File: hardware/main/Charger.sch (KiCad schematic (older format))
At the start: 74 parts, among them K801 DIPxx-1Axx-13x, K802 SANYOU_SRD_Form_C, Q801 BCV27, Q802 Q_NPN_BEC, Q803 BCV27, U801 LM7812

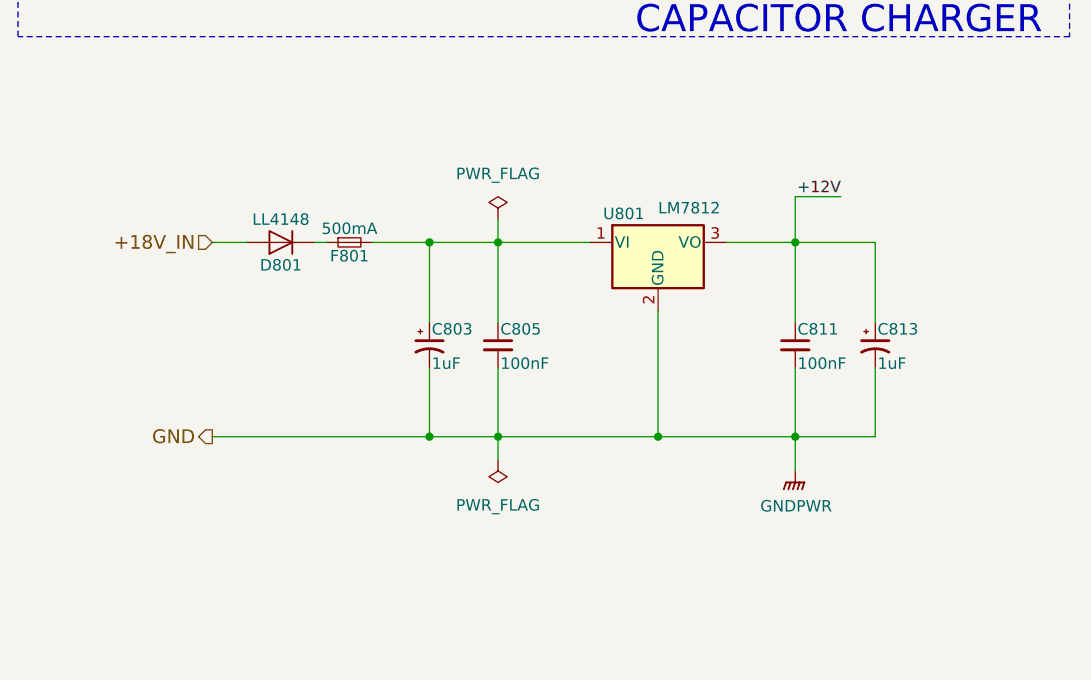
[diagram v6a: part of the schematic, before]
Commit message: Copper bar fixation
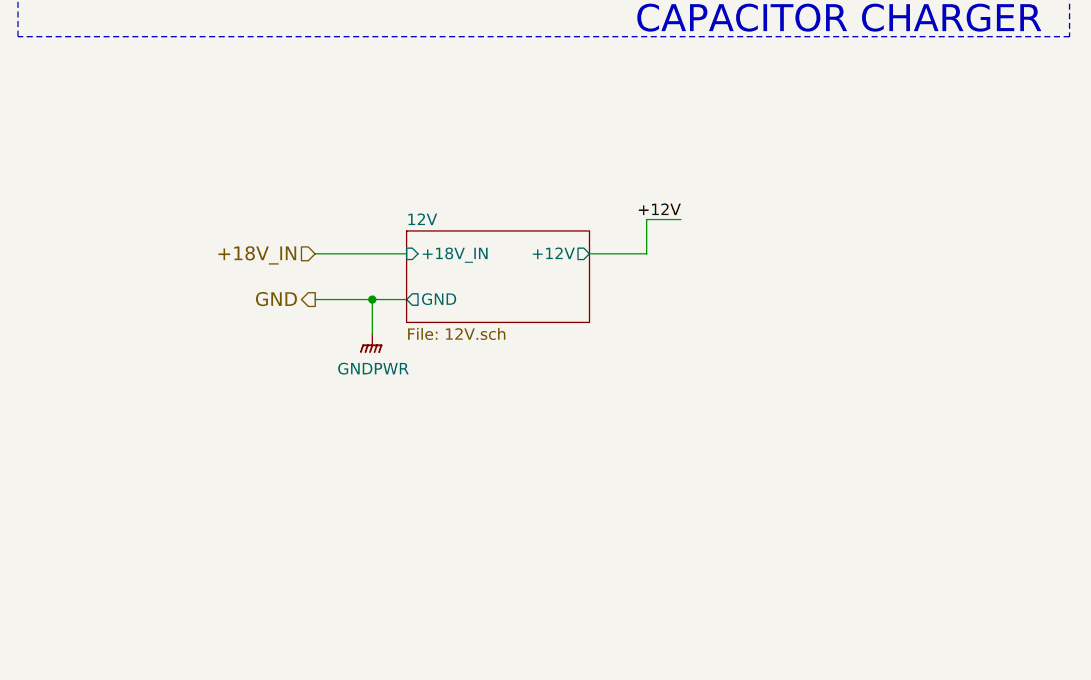
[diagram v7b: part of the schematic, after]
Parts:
- removed C803: 1uF, Capacitor_SMD:C_0805_2012Metric_Pad1.15x1.40mm_HandSolder, symbol Device:CP1_Small
- removed C805, C811: 100nF, Capacitor_SMD:C_0805_2012Metric_Pad1.15x1.40mm_HandSolder, symbol Device:C_Small
- removed C813: 1uF, Capacitor_Tantalum_SMD:CP_EIA-6032-20_AVX-F_Pad2.25x2.35mm_HandSolder, symbol Device:CP1_Small
- removed D801: LL4148, Diode_SMD:D_MiniMELF_Handsoldering, symbol Diode:LL4148
- removed F801: 500mA, Fuse:Fuse_1206_3216Metric_Pad1.42x1.75mm_HandSolder, symbol Device:Fuse_Small
- removed U801: LM7812, Package_SO:SOIC-8_3.9x4.9mm_P1.27mm, symbol Regulator_Linear:LM7805_TO220
- C812: footprint Capacitor_SMD:C_0805_2012Metric_Pad1.15x1.40mm_HandSolder -> Capacitor_THT:CP_Radial_D10.0mm_P5.00mm
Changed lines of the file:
@@
 $Descr A3 16535 11693
 encoding utf-8
-Sheet 2 8
+Sheet 2 9
 Title ""
 Date ""
@@
 F 0 "C812" H 4250 5300 50  0000 L CNN
 F 1 "4700u" H 4250 5250 50  0000 L CNN
-F 2 "Capacitor_SMD:C_0805_2012Metric_Pad1.15x1.40mm_HandSolder" H 4150 5250 50  0001 C CNN
+F 2 "Capacitor_THT:CP_Radial_D10.0mm_P5.00mm" H 4150 5250 50  0001 C CNN
 F 3 "~" H 4150 5250 50  0001 C CNN
 	1    4150 5250
@@
 Wire Wire Line
 	2800 3100 2800 3450
-$Comp
-L Regulator_Linear:LM7805_TO220 U?
-U 1 1 5CB0F970
-P 3450 7600
-AR Path="/5AACFFEF/5CB0F970" Ref="U?"  Part="1"
-AR Path="/5CA4DC1F/5CA5A5C0/5CB0F970" Ref="U?"  Part="1"
-AR Path="/5C9C4D6B/5CB0F970" Ref="U801"  Part="1"
-AR Path="/5CBD2CE3/5CB0F970" Ref="U?"  Part="1"
-F 0 "U801" H 3300 7725 50  0000 C CNN
-F 1 "LM7812" H 3450 7750 50  0000 L CNN
-F 2 "Package_SO:SOIC-8_3.9x4.9mm_P1.27mm" H 3450 7825 50  0001 C CIN
-F 3 "https://www.sparkfun.com/datasheets/Components/LM7805.pdf" H 3450 7550 50  0001 C CNN
-	1    3450 7600
-	1    0    0    -1
-$EndComp
-Text HLabel 1500 8450 0    60   Output ~ 0
+Text HLabel 1950 7850 0    60   Output ~ 0
 GND
-$Comp
-L Device:C_Small C?
-U 1 1 5CB0F97E
-P 2750 8050
-AR Path="/5AACFFEF/5CB0F97E" Ref="C?"  Part="1"
-AR Path="/5CA4DC1F/5CA5A5C0/5CB0F97E" Ref="C?"  Part="1"
-AR Path="/5C9C4D6B/5CB0F97E" Ref="C805"  Part="1"
-AR Path="/5CBD2CE3/5CB0F97E" Ref="C?"  Part="1"
-F 0 "C805" H 2760 8120 50  0000 L CNN
-F 1 "100nF" H 2760 7970 50  0000 L CNN
-F 2 "Capacitor_SMD:C_0805_2012Metric_Pad1.15x1.40mm_HandSolder" H 2750 8050 50  0001 C CNN
-F 3 "" H 2750 8050 50  0001 C CNN
-	1    2750 8050
-	1    0    0    -1
-$EndComp
-$Comp
-L Diode:LL4148 D?
-U 1 1 5CB0F984
-P 1800 7600
-AR Path="/5AACFFEF/5CB0F984" Ref="D?"  Part="1"
-AR Path="/5CA4DC1F/5CA5A5C0/5CB0F984" Ref="D?"  Part="1"
-AR Path="/5C9C4D6B/5CB0F984" Ref="D801"  Part="1"
-AR Path="/5CBD2CE3/5CB0F984" Ref="D?"  Part="1"
-F 0 "D801" H 1800 7700 50  0000 C CNN
-F 1 "LL4148" H 1800 7500 50  0000 C CNN
-F 2 "Diode_SMD:D_MiniMELF_Handsoldering" H 1800 7425 50  0001 C CNN
-F 3 "https://www.vishay.com/docs/85557/ll4148.pdf" H 1800 7600 50  0001 C CNN
-	1    1800 7600
-	-1   0    0    1
-$EndComp
-Text HLabel 1500 7600 0    60   Input ~ 0
+Text HLabel 1950 7650 0    60   Input ~ 0
 +18V_IN
-$Comp
-L Device:C_Small C?
-U 1 1 5CB0F98B
-P 4050 8050
-AR Path="/5AACFFEF/5CB0F98B" Ref="C?"  Part="1"
-AR Path="/5CA4DC1F/5CA5A5C0/5CB0F98B" Ref="C?"  Part="1"
-AR Path="/5C9C4D6B/5CB0F98B" Ref="C811"  Part="1"
-AR Path="/5CBD2CE3/5CB0F98B" Ref="C?"  Part="1"
-F 0 "C811" H 4060 8120 50  0000 L CNN
-F 1 "100nF" H 4060 7970 50  0000 L CNN
-F 2 "Capacitor_SMD:C_0805_2012Metric_Pad1.15x1.40mm_HandSolder" H 4050 8050 50  0001 C CNN
-F 3 "" H 4050 8050 50  0001 C CNN
-	1    4050 8050
-	1    0    0    -1
-$EndComp
-$Comp
-L Device:Fuse_Small F?
-U 1 1 5CB0F997
-P 2100 7600
-AR Path="/5AACFFEF/5CB0F997" Ref="F?"  Part="1"
-AR Path="/5CA4DC1F/5CA5A5C0/5CB0F997" Ref="F?"  Part="1"
-AR Path="/5C9C4D6B/5CB0F997" Ref="F801"  Part="1"
-AR Path="/5CBD2CE3/5CB0F997" Ref="F?"  Part="1"
-F 0 "F801" H 2100 7540 50  0000 C CNN
-F 1 "500mA" H 2100 7660 50  0000 C CNN
-F 2 "Fuse:Fuse_1206_3216Metric_Pad1.42x1.75mm_HandSolder" H 2100 7600 50  0001 C CNN
-F 3 "https://www.mouser.com/datasheet/2/643/0ZCJ_Nov2016-1132002.pdf" H 2100 7600 50  0001 C CNN
-	1    2100 7600
-	1    0    0    -1
-$EndComp
-Wire Wire Line
-	2450 8450 2450 8150
-Connection ~ 2450 7600
-Wire Wire Line
-	2750 8150 2750 8450
-Connection ~ 2450 8450
-Connection ~ 2750 7600
-Wire Wire Line
-	1650 7600 1500 7600
-Connection ~ 2750 8450
-Wire Wire Line
-	3450 8450 3450 7900
-Wire Wire Line
-	4050 8450 4050 8150
-Connection ~ 3450 8450
-Connection ~ 4050 7600
-Wire Wire Line
-	1500 8450 2450 8450
-Wire Wire Line
-	4400 7600 4400 7950
-Wire Wire Line
-	4400 8450 4400 8150
-Connection ~ 4050 8450
-Wire Wire Line
-	2450 7600 2450 7950
-Wire Wire Line
-	2200 7600 2450 7600
-Wire Wire Line
-	2450 7600 2750 7600
-Wire Wire Line
-	2450 8450 2750 8450
-Wire Wire Line
-	2750 7600 2750 7950
-Wire Wire Line
-	2750 7600 3150 7600
-Wire Wire Line
-	2750 8450 2750 8550
-Wire Wire Line
-	2750 8450 3450 8450
-Wire Wire Line
-	3450 8450 4050 8450
-Wire Wire Line
-	4050 7600 4400 7600
-Wire Wire Line
-	4050 7600 4050 7950
-Wire Wire Line
-	4050 8450 4400 8450
-Wire Wire Line
-	1950 7600 2000 7600
-$Comp
-L power:PWR_FLAG #FLG?
-U 1 1 5CB0F9BC
-P 2750 7500
-AR Path="/5AACFFEF/5CB0F9BC" Ref="#FLG?"  Part="1"
-AR Path="/5CA4DC1F/5CA5A5C0/5CB0F9BC" Ref="#FLG?"  Part="1"
-AR Path="/5C9C4D6B/5CB0F9BC" Ref="#FLG0802"  Part="1"
-AR Path="/5CBD2CE3/5CB0F9BC" Ref="#FLG?"  Part="1"
-F 0 "#FLG0802" H 2750 7575 50  0001 C CNN
-F 1 "PWR_FLAG" H 2750 7700 50  0000 C CNN
-F 2 "" H 2750 7500 50  0001 C CNN
-F 3 "~" H 2750 7500 50  0001 C CNN
-	1    2750 7500
-	1    0    0    -1
-$EndComp
-$Comp
-L power:PWR_FLAG #FLG?
-U 1 1 5CB0F9C2
-P 2750 8550
-AR Path="/5AACFFEF/5CB0F9C2" Ref="#FLG?"  Part="1"
-AR Path="/5CA4DC1F/5CA5A5C0/5CB0F9C2" Ref="#FLG?"  Part="1"
-AR Path="/5C9C4D6B/5CB0F9C2" Ref="#FLG0803"  Part="1"
-AR Path="/5CBD2CE3/5CB0F9C2" Ref="#FLG?"  Part="1"
-F 0 "#FLG0803" H 2750 8625 50  0001 C CNN
-F 1 "PWR_FLAG" H 2750 8750 50  0000 C CNN
-F 2 "" H 2750 8550 50  0001 C CNN
-F 3 "~" H 2750 8550 50  0001 C CNN
-	1    2750 8550
-	-1   0    0    1
-$EndComp
-Wire Wire Line
-	2750 7500 2750 7600
-$Comp
-L Device:CP1_Small C?
-U 1 1 5CB0F978
-P 2450 8050
-AR Path="/5AACFFEF/5CB0F978" Ref="C?"  Part="1"
-AR Path="/5CA4DC1F/5CA5A5C0/5CB0F978" Ref="C?"  Part="1"
-AR Path="/5C9C4D6B/5CB0F978" Ref="C803"  Part="1"
-AR Path="/5CBD2CE3/5CB0F978" Ref="C?"  Part="1"
-F 0 "C803" H 2460 8120 50  0000 L CNN
-F 1 "1uF" H 2460 7970 50  0000 L CNN
-F 2 "Capacitor_SMD:C_0805_2012Metric_Pad1.15x1.40mm_HandSolder" H 2450 8050 50  0001 C CNN
-F 3 "" H 2450 8050 50  0001 C CNN
-	1    2450 8050
-	1    0    0    -1
-$EndComp
-$Comp
-L Device:CP1_Small C?
-U 1 1 5CB0F991
-P 4400 8050
-AR Path="/5AACFFEF/5CB0F991" Ref="C?"  Part="1"
-AR Path="/5CA4DC1F/5CA5A5C0/5CB0F991" Ref="C?"  Part="1"
-AR Path="/5C9C4D6B/5CB0F991" Ref="C813"  Part="1"
-AR Path="/5CBD2CE3/5CB0F991" Ref="C?"  Part="1"
-F 0 "C813" H 4410 8120 50  0000 L CNN
-F 1 "1uF" H 4410 7970 50  0000 L CNN
-F 2 "Capacitor_Tantalum_SMD:CP_EIA-6032-20_AVX-F_Pad2.25x2.35mm_HandSolder" H 4400 8050 50  0001 C CNN
-F 3 "" H 4400 8050 50  0001 C CNN
-	1    4400 8050
-	1    0    0    -1
-$EndComp
-Wire Wire Line
-	4250 7400 4050 7400
-Wire Wire Line
-	4050 7400 4050 7600
-Text Label 4250 7400 2    50   ~ 0
-+12V
 Wire Wire Line
 	7700 4900 7700 5250
-$Comp
-L power:GNDPWR #PWR0804
-U 1 1 5CB769FE
-P 4050 8600
-AR Path="/5C9C4D6B/5CB769FE" Ref="#PWR0804"  Part="1"
-AR Path="/5CBD2CE3/5CB769FE" Ref="#PWR?"  Part="1"
-F 0 "#PWR0804" H 4050 8400 50  0001 C CNN
-F 1 "GNDPWR" H 4054 8446 50  0000 C CNN
-F 2 "" H 4050 8550 50  0001 C CNN
-F 3 "" H 4050 8550 50  0001 C CNN
-	1    4050 8600
-	1    0    0    -1
-$EndComp
-Wire Wire Line
-	4050 8600 4050 8450
 $Comp
 L power:PWR_FLAG #FLG0801
@@
 Wire Wire Line
 	1950 2600 2050 2600
-Wire Wire Line
-	3750 7600 4050 7600
 $Comp
 L power:PWR_FLAG #FLG0101
@@
 	1    0    0    -1
 $EndComp
+$Sheet
+S 2350 7550 800  400
+U 5CA70307
+F0 "12V" 50
+F1 "12V.sch" 50
+F2 "+18V_IN" I L 2350 7650 50
+F3 "GND" O L 2350 7850 50
+F4 "+12V" O R 3150 7650 50
+$EndSheet
+Wire Wire Line
+	1950 7850 2200 7850
+$Comp
+L power:GNDPWR #PWR?
+U 1 1 5CA8D58E
+P 2200 8000
+AR Path="/5C9C4D6B/5CA8D58E" Ref="#PWR?"  Part="1"
+AR Path="/5CBD2CE3/5CA8D58E" Ref="#PWR?"  Part="1"
+F 0 "#PWR?" H 2200 7800 50  0001 C CNN
+F 1 "GNDPWR" H 2204 7846 50  0000 C CNN
+F 2 "" H 2200 7950 50  0001 C CNN
+F 3 "" H 2200 7950 50  0001 C CNN
+	1    2200 8000
+	1    0    0    -1
+$EndComp
+Wire Wire Line
+	2200 8000 2200 7850
+Connection ~ 2200 7850
+Wire Wire Line
+	2200 7850 2350 7850
+Wire Wire Line
+	1950 7650 2350 7650
+Wire Wire Line
+	3150 7650 3400 7650
+Wire Wire Line
+	3400 7650 3400 7500
+Wire Wire Line
+	3400 7500 3550 7500
+Text Label 3550 7500 2    50   ~ 0
++12V
 $EndSCHEMATC

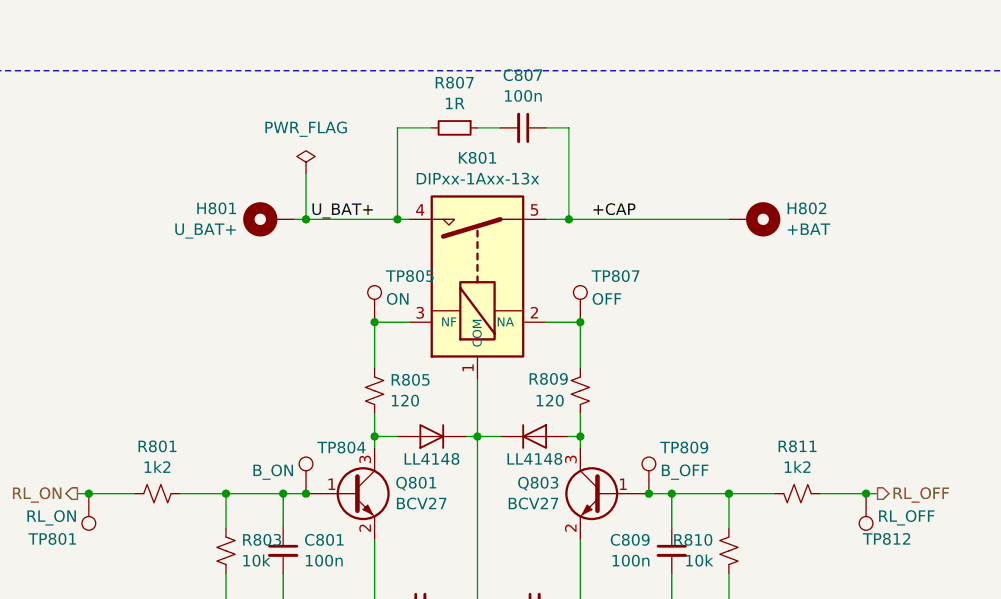
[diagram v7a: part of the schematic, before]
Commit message: Layout and Relay footprint
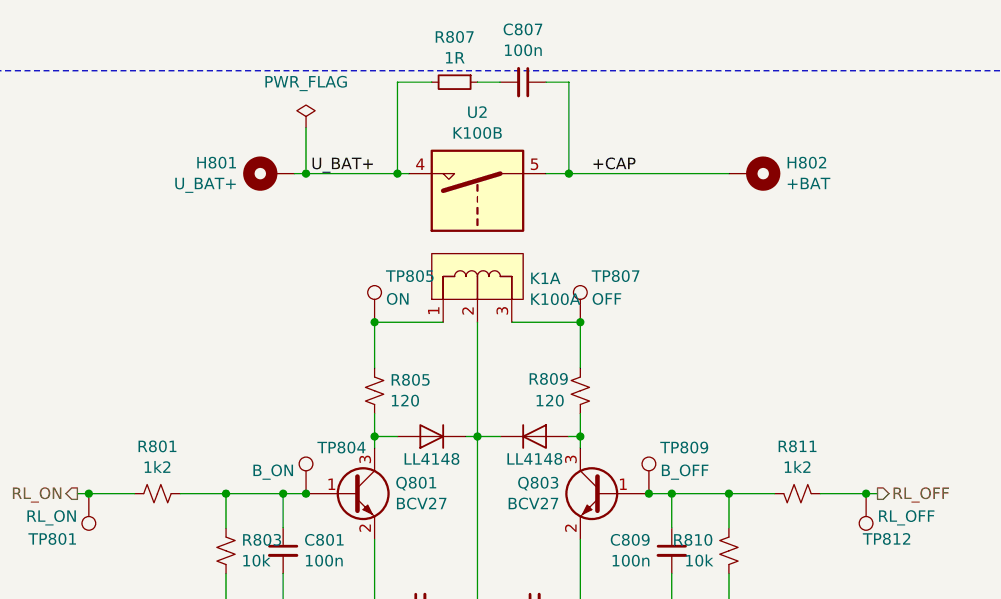
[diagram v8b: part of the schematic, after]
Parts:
- removed K801: DIPxx-1Axx-13x, KicadZeniteSolarLibrary18:Mega_Relay_K100, symbol main-rescue:DIPxx-1Axx-13x-High_current_rele
- added K1: K100A, Connector_PinHeader_2.54mm:PinHeader_1x03_P2.54mm_Vertical_SMD_Pin1Right, symbol K100:K100A
- added U2: K100B, KicadZeniteSolarLibrary18:Mega_Relay_K100_separated, symbol k100A:K100B
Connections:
- net +12V: now also K1.2
- net +CAP: now also U2.5
- net U_BAT+: now also U2.4
- net at R809.1, TP807.1: now also K1.3
- net at R805.1, TP805.1: now also K1.1
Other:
- moved on the sheet: C807, H801, H802, R807
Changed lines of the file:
@@
-$EndComp
-$Comp
-L main-rescue:DIPxx-1Axx-13x-High_current_rele K?
-U 1 1 5C9E2F33
-P 2800 1600
-AR Path="/5C9E2F33" Ref="K?"  Part="1"
-AR Path="/5C9C4D6B/5C9E2F33" Ref="K801"  Part="1"
-AR Path="/5CBD2CE3/5C9E2F33" Ref="K?"  Part="1"
-F 0 "K801" V 3267 1600 50  0000 C CNN
-F 1 "DIPxx-1Axx-13x" V 3176 1600 50  0000 C CNN
-F 2 "KicadZeniteSolarLibrary18:Mega_Relay_K100" H 3150 1550 50  0001 L CNN
-F 3 "https://standexelectronics.com/wp-content/uploads/datasheet_reed_relay_DIP.pdf" H 2800 1600 50  0001 C CNN
-	1    2800 1600
-	0    -1   -1   0
 $EndComp
 $Comp
@@
 	2350 2050 2350 1850
 Wire Wire Line
-	2350 1850 2500 1850
-Wire Wire Line
 	2350 2250 2350 2350
 $Comp
@@
 	3250 2050 3250 1850
 Wire Wire Line
-	3250 1850 3100 1850
-Wire Wire Line
 	3250 2250 3250 2350
 $Comp
@@
 Wire Wire Line
 	3650 3150 3650 3100
-Text Label 2350 1400 2    50   ~ 0
+Text Label 2350 1200 2    50   ~ 0
 U_BAT+
 $Comp
 L Mechanical:MountingHole_Pad H802
 U 1 1 5C9E3AC0
-P 4000 1400
+P 4000 1200
 AR Path="/5C9C4D6B/5C9E3AC0" Ref="H802"  Part="1"
 AR Path="/5CBD2CE3/5C9E3AC0" Ref="H?"  Part="1"
-F 0 "H802" V 3954 1550 50  0000 L CNN
-F 1 "+BAT" V 4045 1550 50  0000 L CNN
-F 2 "MountingHole:MountingHole_3.2mm_M3_DIN965_Pad" H 4000 1400 50  0001 C CNN
-F 3 "~" H 4000 1400 50  0001 C CNN
-	1    4000 1400
+F 0 "H802" V 3954 1350 50  0000 L CNN
+F 1 "+BAT" V 4045 1350 50  0000 L CNN
+F 2 "MountingHole:MountingHole_3.2mm_M3_DIN965_Pad" H 4000 1200 50  0001 C CNN
+F 3 "~" H 4000 1200 50  0001 C CNN
+	1    4000 1200
 	0    1    1    0
 $EndComp
@@
 L Mechanical:MountingHole_Pad H801
 U 1 1 5CA4A13E
-P 1900 1400
+P 1900 1200
 AR Path="/5C9C4D6B/5CA4A13E" Ref="H801"  Part="1"
 AR Path="/5CBD2CE3/5CA4A13E" Ref="H?"  Part="1"
-F 0 "H801" V 1854 1550 50  0000 L CNN
-F 1 "U_BAT+" V 1945 1550 50  0000 L CNN
-F 2 "MountingHole:MountingHole_3.2mm_M3_DIN965_Pad" H 1900 1400 50  0001 C CNN
-F 3 "~" H 1900 1400 50  0001 C CNN
-	1    1900 1400
+F 0 "H801" V 1854 1350 50  0000 L CNN
+F 1 "U_BAT+" V 1945 1350 50  0000 L CNN
+F 2 "MountingHole:MountingHole_3.2mm_M3_DIN965_Pad" H 1900 1200 50  0001 C CNN
+F 3 "~" H 1900 1200 50  0001 C CNN
+	1    1900 1200
 	0    -1   1    0
 $EndComp
@@
 $EndComp
 Wire Wire Line
-	2000 1400 2050 1400
+	2000 1200 2050 1200
 $Comp
 L power:GNDPWR #PWR0810
@@
 Wire Wire Line
 	4150 5450 4150 5500
-Wire Wire Line
-	2800 2100 2800 2350
 Text Label 3000 3450 2    50   ~ 0
 +12V
@@
 L power:PWR_FLAG #FLG0801
 U 1 1 5CB83AF7
-P 2050 1200
+P 2050 1000
 AR Path="/5C9C4D6B/5CB83AF7" Ref="#FLG0801"  Part="1"
 AR Path="/5CBD2CE3/5CB83AF7" Ref="#FLG?"  Part="1"
-F 0 "#FLG0801" H 2050 1275 50  0001 C CNN
-F 1 "PWR_FLAG" H 2050 1400 50  0000 C CNN
-F 2 "" H 2050 1200 50  0001 C CNN
-F 3 "~" H 2050 1200 50  0001 C CNN
-	1    2050 1200
-	1    0    0    -1
-$EndComp
-Wire Wire Line
-	2050 1200 2050 1400
-Connection ~ 2050 1400
-Wire Wire Line
-	2050 1400 2450 1400
+F 0 "#FLG0801" H 2050 1075 50  0001 C CNN
+F 1 "PWR_FLAG" H 2050 1200 50  0000 C CNN
+F 2 "" H 2050 1000 50  0001 C CNN
+F 3 "~" H 2050 1000 50  0001 C CNN
+	1    2050 1000
+	1    0    0    -1
+$EndComp
+Wire Wire Line
+	2050 1000 2050 1200
+Connection ~ 2050 1200
+Wire Wire Line
+	2050 1200 2450 1200
 $Comp
 L power:PWR_FLAG #FLG0804
@@
 L Device:R_Small R807
 U 1 1 5CA4B635
-P 2700 1000
-F 0 "R807" V 2504 1000 50  0000 C CNN
-F 1 "1R" V 2595 1000 50  0000 C CNN
-F 2 "Resistor_SMD:R_0805_2012Metric_Pad1.15x1.40mm_HandSolder" H 2700 1000 50  0001 C CNN
-F 3 "~" H 2700 1000 50  0001 C CNN
-	1    2700 1000
+P 2700 800
+F 0 "R807" V 2504 800 50  0000 C CNN
+F 1 "1R" V 2595 800 50  0000 C CNN
+F 2 "Resistor_SMD:R_0805_2012Metric_Pad1.15x1.40mm_HandSolder" H 2700 800 50  0001 C CNN
+F 3 "~" H 2700 800 50  0001 C CNN
+	1    2700 800
 	0    1    1    0
 $EndComp
@@
 L Device:C_Small C807
 U 1 1 5CA4B63B
-P 3000 1000
-F 0 "C807" V 2771 1000 50  0000 C CNN
-F 1 "100n" V 2862 1000 50  0000 C CNN
-F 2 "Capacitor_SMD:C_0805_2012Metric_Pad1.15x1.40mm_HandSolder" H 3000 1000 50  0001 C CNN
-F 3 "~" H 3000 1000 50  0001 C CNN
-	1    3000 1000
+P 3000 800
+F 0 "C807" V 2771 800 50  0000 C CNN
+F 1 "100n" V 2862 800 50  0000 C CNN
+F 2 "Capacitor_SMD:C_0805_2012Metric_Pad1.15x1.40mm_HandSolder" H 3000 800 50  0001 C CNN
+F 3 "~" H 3000 800 50  0001 C CNN
+	1    3000 800
 	0    1    1    0
 $EndComp
 Wire Wire Line
-	2800 1000 2900 1000
-Wire Wire Line
-	2450 1000 2450 1400
-Wire Wire Line
-	2450 1000 2600 1000
-Connection ~ 2450 1400
-Wire Wire Line
-	2450 1400 2500 1400
-Wire Wire Line
-	3200 1000 3200 1400
-Wire Wire Line
-	3100 1400 3200 1400
-Wire Wire Line
-	3100 1000 3200 1000
-Connection ~ 3200 1400
-Wire Wire Line
-	3200 1400 3900 1400
+	2800 800  2900 800
+Wire Wire Line
+	2450 800  2450 1200
+Wire Wire Line
+	2450 800  2600 800
+Connection ~ 2450 1200
+Wire Wire Line
+	2450 1200 2500 1200
+Wire Wire Line
+	3200 800  3200 1200
+Wire Wire Line
+	3100 1200 3200 1200
+Wire Wire Line
+	3100 800  3200 800
+Connection ~ 3200 1200
+Wire Wire Line
+	3200 1200 3900 1200
 $Comp
 L Device:R_Small R808
@@
 	8000 8000 7950 8000
 Connection ~ 7950 8000
-Text Label 3300 1400 0    50   ~ 0
+Text Label 3300 1200 0    50   ~ 0
 +CAP
 Connection ~ 2050 5700
@@
 	1950 7850 2200 7850
 $Comp
-L power:GNDPWR #PWR?
+L power:GNDPWR #PWR0101
 U 1 1 5CA8D58E
 P 2200 8000
-AR Path="/5C9C4D6B/5CA8D58E" Ref="#PWR?"  Part="1"
+AR Path="/5C9C4D6B/5CA8D58E" Ref="#PWR0101"  Part="1"
 AR Path="/5CBD2CE3/5CA8D58E" Ref="#PWR?"  Part="1"
-F 0 "#PWR?" H 2200 7800 50  0001 C CNN
+F 0 "#PWR0101" H 2200 7800 50  0001 C CNN
 F 1 "GNDPWR" H 2204 7846 50  0000 C CNN
 F 2 "" H 2200 7950 50  0001 C CNN
@@
 Text Label 3550 7500 2    50   ~ 0
 +12V
+Wire Wire Line
+	2350 1850 2650 1850
+Wire Wire Line
+	2950 1850 3250 1850
+Wire Wire Line
+	2800 1850 2800 2350
+$Comp
+L K100:K100A K1
+U 1 1 5CA93DA7
+P 2800 1750
+F 0 "K1" V 2890 1522 50  0000 R CNN
+F 1 "K100A" V 2799 1522 50  0000 R CNN
+F 2 "Connector_PinHeader_2.54mm:PinHeader_1x03_P2.54mm_Vertical_SMD_Pin1Right" H 3150 1700 50  0001 L CNN
+F 3 "https://standexelectronics.com/wp-content/uploads/datasheet_reed_relay_SIL.pdf" H 2800 1750 50  0001 C CNN
+	1    2800 1750
+	0    -1   -1   0
+$EndComp
+$Comp
+L k100A:K100B U2
+U 1 1 5CA9433B
+P 2800 1350
+F 0 "U2" V 3217 1350 50  0000 C CNN
+F 1 "K100B" V 3126 1350 50  0000 C CNN
+F 2 "KicadZeniteSolarLibrary18:Mega_Relay_K100_separated" H 2550 1200 50  0001 C CNN
+F 3 "" H 2550 1200 50  0001 C CNN
+	1    2800 1350
+	0    -1   -1   0
+$EndComp
 $EndSCHEMATC
